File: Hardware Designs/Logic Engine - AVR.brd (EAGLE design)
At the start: 61 x 35.6 mm, 44 parts, among them IC1 MEGA328P, U1 LP2985, U2 HEX_CONVERTER, Y1 16MHz

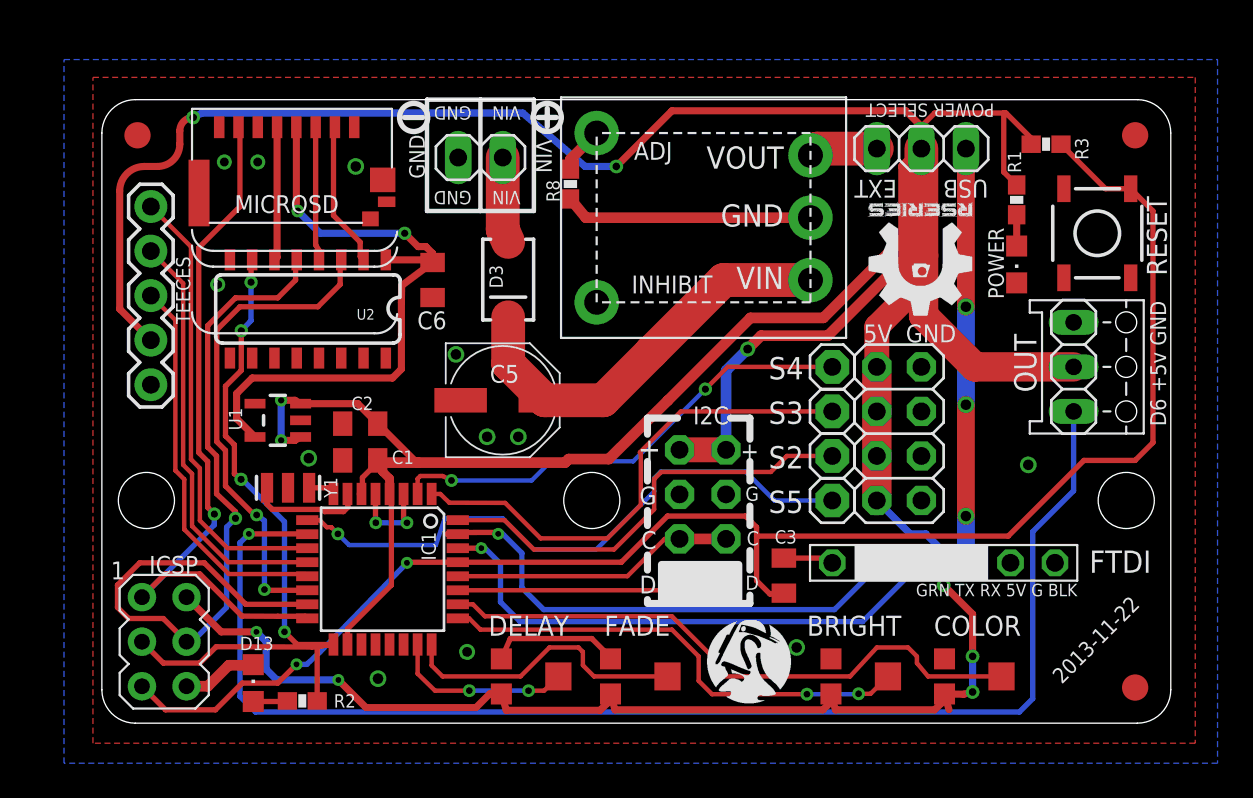
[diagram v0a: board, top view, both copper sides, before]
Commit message: Updated AVR board to production version
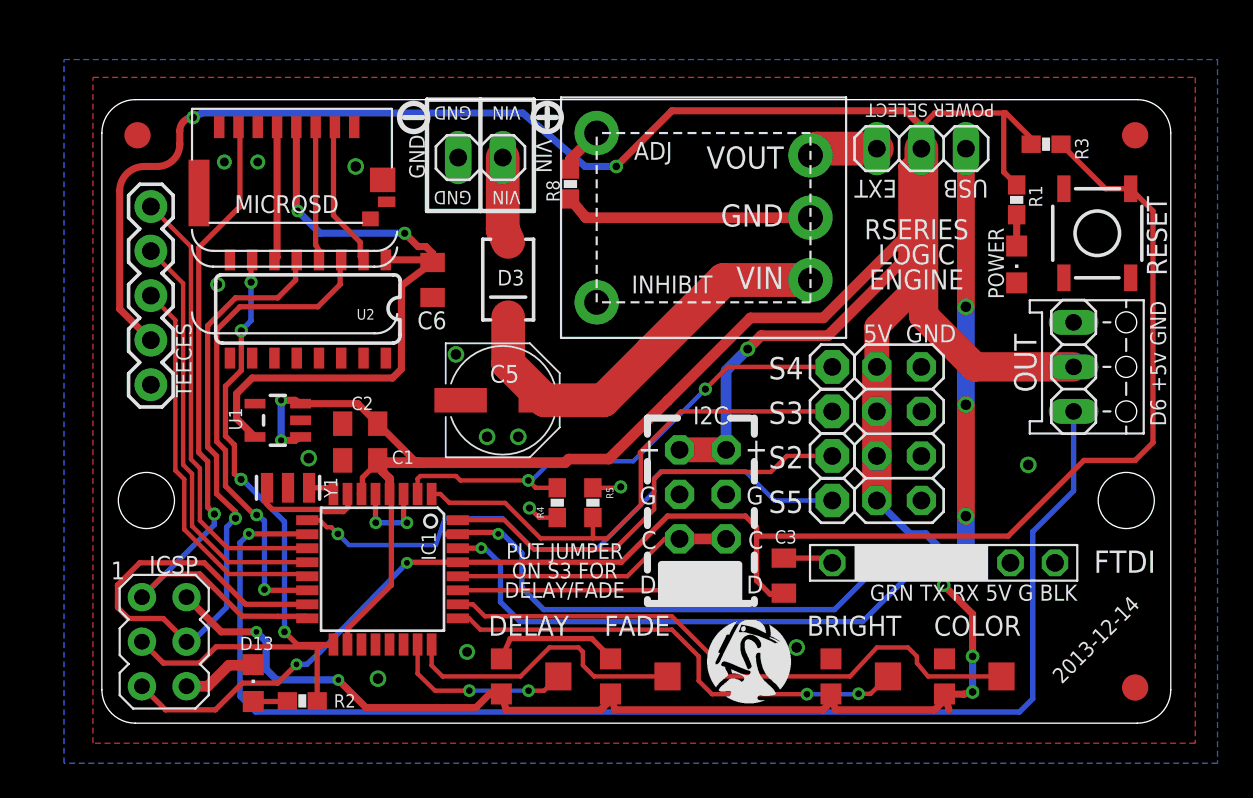
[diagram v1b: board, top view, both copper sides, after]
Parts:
- removed U$2: (no value), rseries:RSERIES-OSHW-LOGO-SMALL
- added R4, R5: 10K, SparkFun-Resistors:0603-RES
- FTDI: value GRN TX RX 5V G BLK -> GRN TX RX 5V G BLK
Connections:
- net DIGITAL3: now also R5.2
- net DIGITAL4: now also R4.2
- net GND: now also R4.1, R5.1
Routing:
- net GND: track 31.2 -> 34.7 mm, vias 14 -> 16
- net DIGITAL4: track 27.3 -> 29.2 mm
- net DIGITAL3: track 28.7 -> 29.9 mm
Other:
- board text added: "2013-12-14"
- board text added: "PUT JUMPER ON S3 FOR DELAY/FADE"
- board text added: "RSERIES LOGIC ENGINE"
- board text added: "big thanks to: Michael Erwin, Brett Bourbin & John Vannoy"
- board text removed: "2013-11-22"
- board text removed: "big thanks to: Michael Erwin, Brett Bourbin, John Vannoy, OSHpark.com and SmallBatchAssembly.com"

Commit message: Updated AVR board slightly
Small revision to AVR board for late 2015 run (first change since these
boards were first run). Added resistor on LED output, removed reset
switch, removed 'power' jumper, moved stuff around, routed a little
smarter (I think), added fancy silkscreen art. Functionality-wise this
is identical to the previous version.
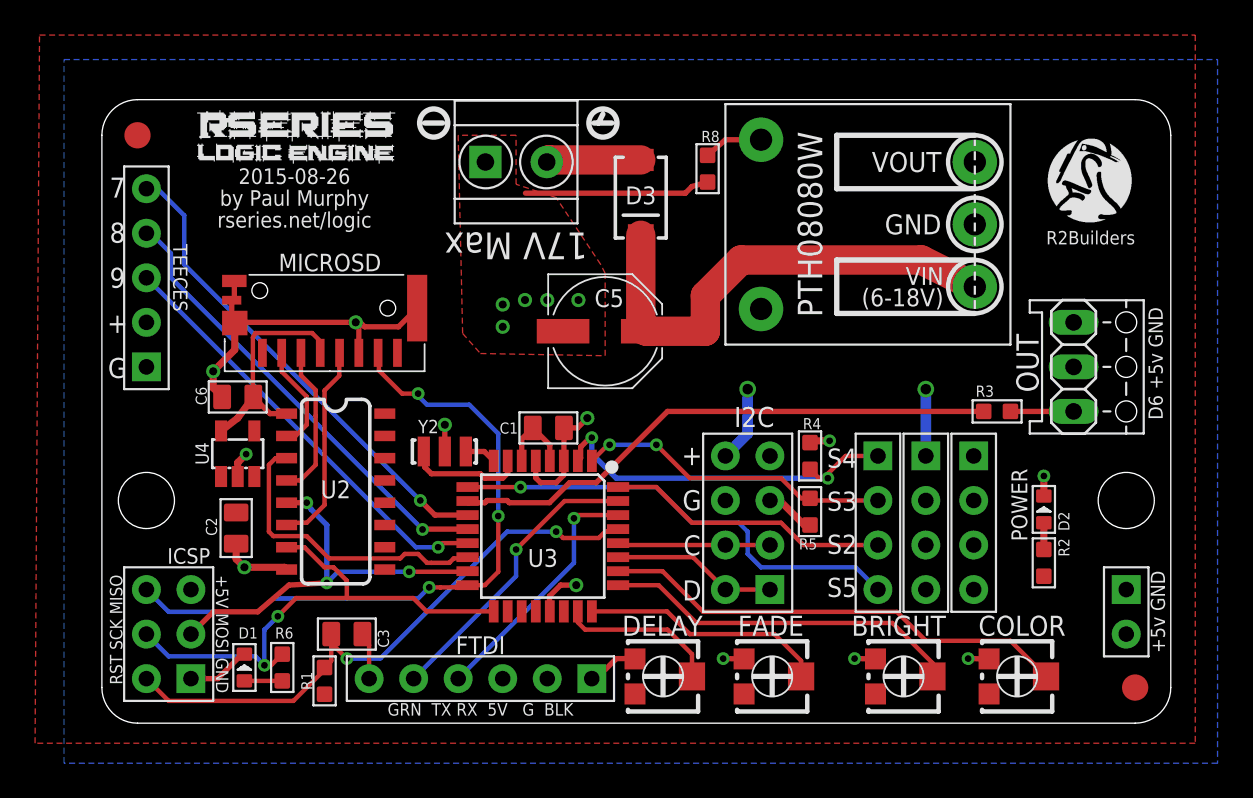
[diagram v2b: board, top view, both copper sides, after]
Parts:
- removed D13: RED, adafruit:CHIPLED_0805
- removed EXT_PWR: (no value), pinhead:1X02
- removed FID5: (no value), SmallBatchLibPre1:FIDUCIAL_G15
- removed I2C, I2C1: (no value), carduino:1X04-CB
- removed IC1: MEGA328P, avr-7:TQFP32-08
- removed JP1: (no value), adafruit:2X04
- removed POWER: GREEN, adafruit:CHIPLED_0805
- removed PWR_SEL1: (no value), pinhead:1X03
- removed RESET: RST, SparkFun-Electromechanical:TACTILE_SWITCH_SMD
- removed S2, S3, S4, S5: (no value), adafruit:1X01
- removed U$5: (no value), rseries:R2BUILDERS-LOGO
- removed U1: LP2985, SparkFun-PowerIC:SOT23-5
- removed Y1: 16MHz, SparkFun-FreqCtrl:RESONATOR-SMD
- added D1, D2: SMD-LED-CLEAR-BLUE(0603), OPL-Diode:LED-0603
- added J1: (no value), OPL-Connector:H2X4-2.54
- added J2, J3, J4: (no value), OPL-Connector:H4-2.54
- added J5: (no value), OPL-Connector:H2-3.5-7.0X7.0MM
- added J6: (no value), OPL-Connector:H2-2.54
- added R6: 1K, OPL-Resistor:R0603
- added U$2: (no value), rseries:RSERIES-LE-LOGO2
- added U3: (no value), Seeed-OPL-ic:TQFP32-0.8-7X7MM
- added U4: 3.3V-150MA, Seeed-OPL-ic:SOT-23-5
- added Y2: 16MHZ, Seeed-OPL-crystal-osctllator:X3-SMD-3.6X1.3X0.8MM
- C1, C2, C3: value 0.1uF -> 100nf; device adafruit:C0805K -> Seeed-OPL-Capacitor:C0805
- C5: value 100uF -> 120uf; device adafruit:PANASONIC_D -> rseries:PANASONIC_D
- C6: value 10uF -> 10uf; device adafruit:C0805K -> Seeed-OPL-Capacitor:C0805
- D3: value BA340LA -> SSA33L-E3/5AT
- FTDI: value GRN TX RX 5V G BLK -> (none); device carduino:1X06-CLEAN -> Seeed-OPL-Connector:H6-2.54
- ICSP: value AVRISP-6 -> (none); device adafruit:AVRISP -> Seeed-OPL-Connector:H2X3-2.54
- MICROSD: value MICROSD -> MICROSD47579-001; device rseries:MICROSD_SMALL -> rseries:SD-47579-001
- OUT: value (none) -> MDF7-3S-2.54DSA(55)
- R1: value 1K -> 10K; device SparkFun-Resistors:0603-RES -> OPL-Resistor:R0603
- R2, R4, R5: device SparkFun-Resistors:0603-RES -> OPL-Resistor:R0603
- R3: value 10K -> 348; device SparkFun-Resistors:0603-RES -> Seeed-OPL-Resistor:R0603
- R8: device SparkFun-Resistors:0603-RES -> Seeed-OPL-Resistor:R0603
- REG: value PTH08080W -> PTH08080WAH
- TEECES: value G +5V D9 D8 D7 -> 2p-2.54; device SparkFun-Connectors:1X05 -> Seeed-OPL-Connector:H5-2.54
- U$1: device SparkFun-Aesthetics:OSHW-LOGO-M -> rseries:R2BUILDERS-LOGO
- U$3: device rseries:RSERIES-OSHW-LOGO-MEDIUM-BOTTOM -> rseries:RSERIES-LE-LOGO
- U$4: device rseries:R2BUILDERS-LOGO -> rseries:R2-2LEG
- U2: value HEX_CONVERTER -> 74HC4050D,653
- moved R1 48.1 mm to (12.7, 2.41), turned to 180 degrees
- moved R2 43.0 mm to (53.7, 9.14), turned to 0 degrees
- moved U$1 30.6 mm to (53.8, 28.4), flipped to the top
- moved FTDI 27.2 mm to (21.6, 2.54), turned to 270 degrees
- moved U$4 25.7 mm to (14.4, 5.33)
- moved C3 25.1 mm to (14.0, 5.08)
- moved U$3 21.8 mm to (39.0, 27.8)
- moved R3 15.5 mm to (51.1, 17.8), turned to 90 degrees
- moved R4 14.7 mm to (40.4, 15.2), turned to 0 degrees
- moved MICROSD 13.9 mm to (13.0, 20.3), turned to 180 degrees
- moved C6 13.0 mm to (7.75, 18.6)
- moved R5 12.4 mm to (40.4, 12.1), turned to 180 degrees
- moved C1 10.9 mm to (25.5, 16.8), turned to 90 degrees
- moved U2 10.5 mm to (13.3, 13.2), turned to 270 degrees
- moved REG 9.38 mm to (43.7, 28.4)
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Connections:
- removed net N$1: IC1.7, Y1.1
- removed net N$11: D3.A, EXT_PWR.2
- removed net N$16: MICROSD.3, U2.4
- removed net N$17: MICROSD.5, U2.6
- removed net N$18: MICROSD.2, U2.2
- removed net N$2: IC1.8, Y1.3
- removed net N$21: PWR_SEL1.1, REG.VOUT
- removed net USB_5V: FTDI.3, PWR_SEL1.3
- removed net VDD: C6.1, MICROSD.4, U1.5, U2.1
- new net +3.3V: C6.1, MICROSD.P4, U2.1, U4.5
- new net CS: MICROSD.P2, U2.2
- new net DATA_IN: MICROSD.P3, U2.4
- new net N$10: U3.8, Y2.3
- new net N$7: OUT.3, R3.2
- new net N$9: U3.7, Y2.1
- new net SCLK: MICROSD.P5, U2.6
- new net VIN: D3.A, J5.2
- net +5V: now also FTDI.3, ICSP.3, J1.4, J1.5, J3.1, J3.2, J3.3, J3.4, J6.2, R2.2, REG.VOUT, U3.18, U3.4, U3.6, U4.1, U4.3; no longer I2C.4, I2C1.4, IC1.18, IC1.4, IC1.6, ICSP.2, JP1.1, JP1.3, JP1.5, JP1.7, PWR_SEL1.2, R3.1, U1.1, U1.3
- net ANALOG0: now also U3.23; no longer IC1.23
- net ANALOG1: now also U3.24; no longer IC1.24
- net ANALOG2: now also U3.25; no longer IC1.25
- net ANALOG3: now also U3.26; no longer IC1.26
- net ANALOG4: now also J1.1, J1.8, U3.27; no longer I2C.1, I2C1.1, IC1.27
- net ANALOG5: now also J1.2, J1.7, U3.28; no longer I2C.2, I2C1.2, IC1.28
- net AREF: now also U3.20; no longer IC1.20
- net DIGITAL10: now also U3.14; no longer IC1.14
- net DIGITAL2: now also J2.3, U3.32; no longer IC1.32, S2.1
- net DIGITAL3: now also J2.2, U3.1; no longer IC1.1, S3.1
- net DIGITAL4: now also J2.1, U3.2; no longer IC1.2, S4.1
- net DIGITAL5: now also J2.4, U3.9; no longer IC1.9, S5.1
- net DIGITAL6: now also R3.1, U3.10; no longer IC1.10, OUT.3
- net DIGITAL7: now also U3.11; no longer IC1.11
- net DIGITAL8: now also U3.12; no longer IC1.12
- net DIGITAL9: now also U3.13; no longer IC1.13
- net GND: now also D1.-, D2.-, ICSP.1, J1.3, J1.6, J4.1, J4.2, J4.3, J4.4, J5.1, J6.1, MICROSD.G1, MICROSD.G2, MICROSD.G3, MICROSD.G4, MICROSD.P6, U3.21, U3.3, U3.5, U4.2, Y2.2; no longer D13.C, EXT_PWR.1, I2C.3, I2C1.3, IC1.21, IC1.3, IC1.5, ICSP.6, JP1.2, JP1.4, JP1.6, JP1.8, MICROSD.6, MICROSD.MT1, MICROSD.MT2, POWER.C, RESET.3, U1.2, Y1.2
- net MISO: now also ICSP.4, MICROSD.P7, U3.16; no longer IC1.16, ICSP.1, MICROSD.7
- net MOSI: now also ICSP.2, U3.15; no longer IC1.15, ICSP.4
- net N$4: now also D1.+, R6.2; no longer D13.A, R2.2
- net N$5: now also D2.+, R2.1; no longer POWER.A, R1.2
- net RST: now also ICSP.6, R1.2, U3.29; no longer IC1.29, ICSP.5, R3.2, RESET.1
- net RXD: now also U3.30; no longer IC1.30
- net SCK: now also ICSP.5, R6.1, U3.17; no longer IC1.17, ICSP.3, R2.1
- net TXD: now also U3.31; no longer IC1.31
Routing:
- net +5V: track 265.1 -> 12.6 mm, vias 10 -> 2
- net RST: track 90.3 -> 34.1 mm
- net DIGITAL6: track 76.1 -> 31.8 mm, vias 1 -> 0
- net VDD: track 36.6 -> 0.00 mm, vias 2 -> 0
- net GND: track 34.7 -> 63.2 mm, vias 16 -> 17
- net USB_5V: track 23.6 -> 0.00 mm, vias 3 -> 0
- net MOSI: track 45.7 -> 23.3 mm, vias 1 -> 3
- net RXD: track 30.8 -> 14.5 mm
- net +3.3V: track 0.00 -> 13.3 mm
- net TXD: track 29.4 -> 16.7 mm
- net SCK: track 42.2 -> 30.3 mm, vias 4 -> 2
- net DIGITAL3: track 29.9 -> 18.0 mm, vias 0 -> 2
- net SCLK: track 0.00 -> 11.7 mm
- net DIGITAL10: track 28.1 -> 17.5 mm, vias 2 -> 0
- net DIGITAL2: track 25.3 -> 16.2 mm
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- added copper zone on layer 1, net +5V
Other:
- outline, holes or cut-outs redrawn
- board text added: "+ G C D"
- board text added: "+5V MOSI GND"
- board text added: "+5v GND"
- board text added: "17V Max"
- board text added: "2015-08-26 by Paul Murphy rseries.net/logic"
- board text added: "7 8 9 + G"
- board text added: "GRN TX RX 5V G BLK"
- board text added: "I2C"
- board text added: "POWER"
- board text added: "R2Builders"
- board text added: "RST SCK MISO"
- board text added: "S4 S3 S2 S5"
- board text removed: "+"
- board text removed: "2013-12-14"
- board text removed: "5V"
- board text removed: "C"
- board text removed: "D"
- board text removed: "EXT"
- board text removed: "FTDI"
- board text removed: "G"
- board text removed: "POWER SELECT"
- board text removed: "PUT JUMPER ON S3 FOR DELAY/FADE"
- board text removed: "RSERIES LOGIC ENGINE"
- board text removed: "RSeries Logic Engine by Paul Murphy"
- board text removed: "USB"
- board text removed: "big thanks to: Michael Erwin, Brett Bourbin & John Vannoy"
